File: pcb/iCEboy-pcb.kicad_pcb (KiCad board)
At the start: 2 copper layers, 51 x 61 mm, 65 parts, among them J1 DMG-CardEdge, J2 PROG_PORT, Q1 2N7002K, U1 TC74LCXR163245FT, U2 TC74LCXR163245FT, U3 ICE40UP5K-SG48ITR, U4 TPS79901DDCR, U5 TPS79901DDCR, U6 W25Q80DVSSIG, X1 SG-210STF 20MHz

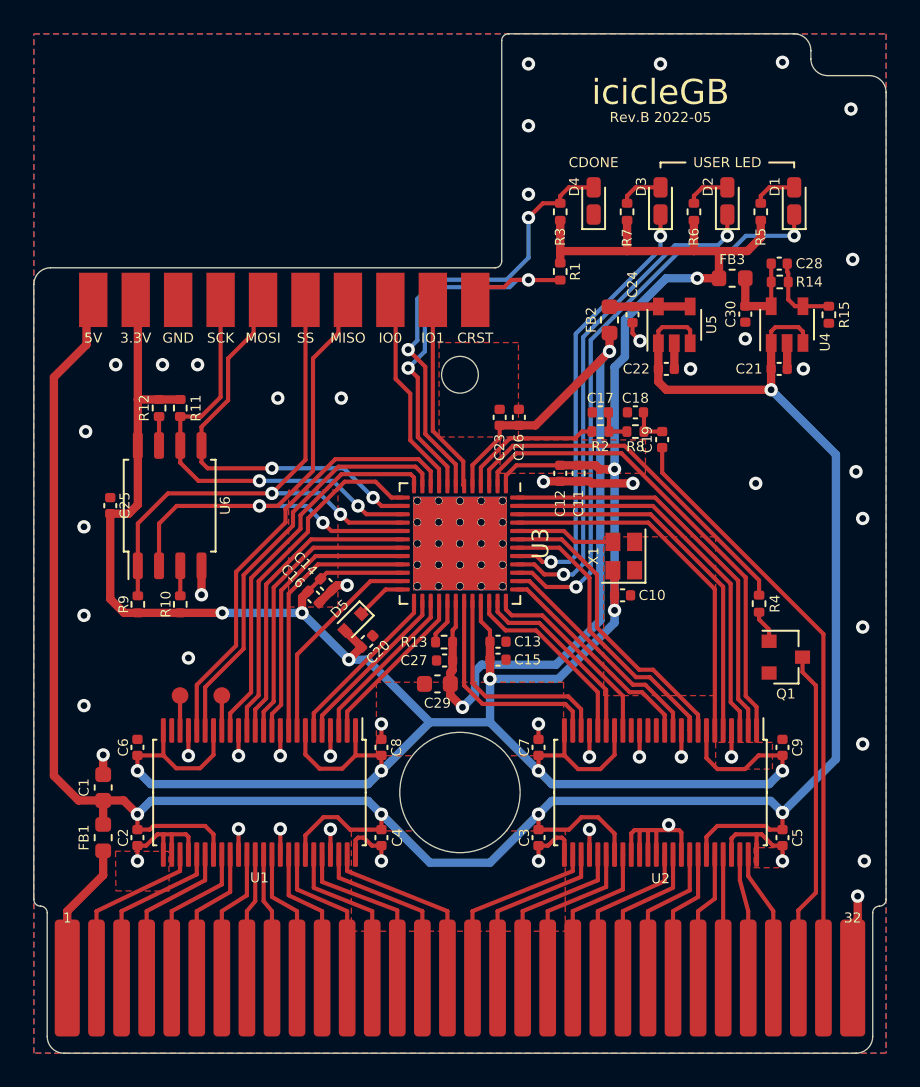
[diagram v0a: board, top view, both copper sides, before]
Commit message: update pcb, drc ok
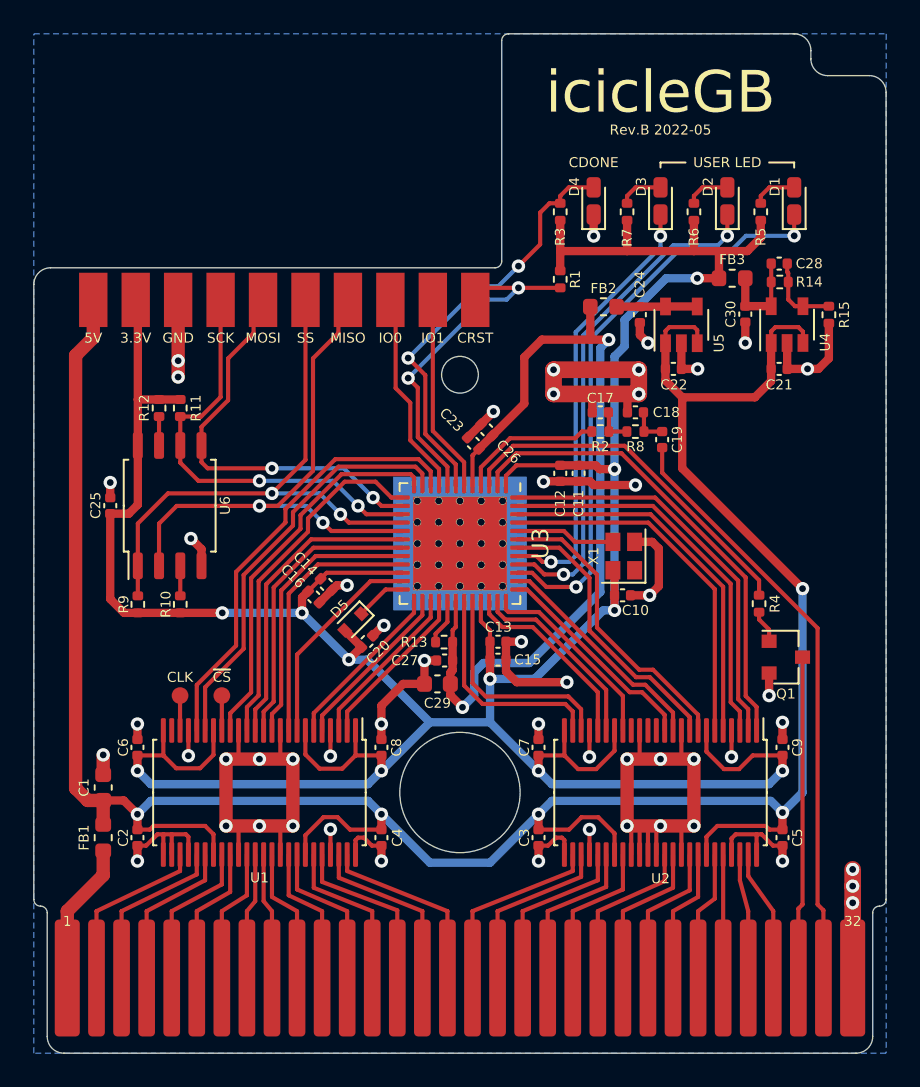
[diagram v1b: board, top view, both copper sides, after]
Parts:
- moved C23 2.21 mm to (60.8, 59.0), turned to 135 degrees
- moved C26 2.07 mm to (61.6, 58.2), turned to 135 degrees
- moved FB2 0.87 mm to (68.6, 50.8), turned to 180 degrees
- moved R1 0.46 mm to (66.0, 49.2)
- moved C24 0.44 mm to (70.8, 51.3)
- moved C22 0.42 mm to (72.8, 54.5)
- moved U5 0.42 mm to (73.2, 51.9)
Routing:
- net GND: track 72.6 -> 158.6 mm, vias 52 -> 53
- net +1V2: track 48.2 -> 50.5 mm
- net /CDONE: track 27.6 -> 25.5 mm
- net /~{CRESET}: track 23.7 -> 21.7 mm
- net +5V: track 154.7 -> 153.6 mm
- net /CB-~{RST}: track 20.0 -> 19.3 mm
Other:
- board text added: "TODO add board information silk"
- board text removed: "TODO relocation / rewiring for 1005 components add board information silk"

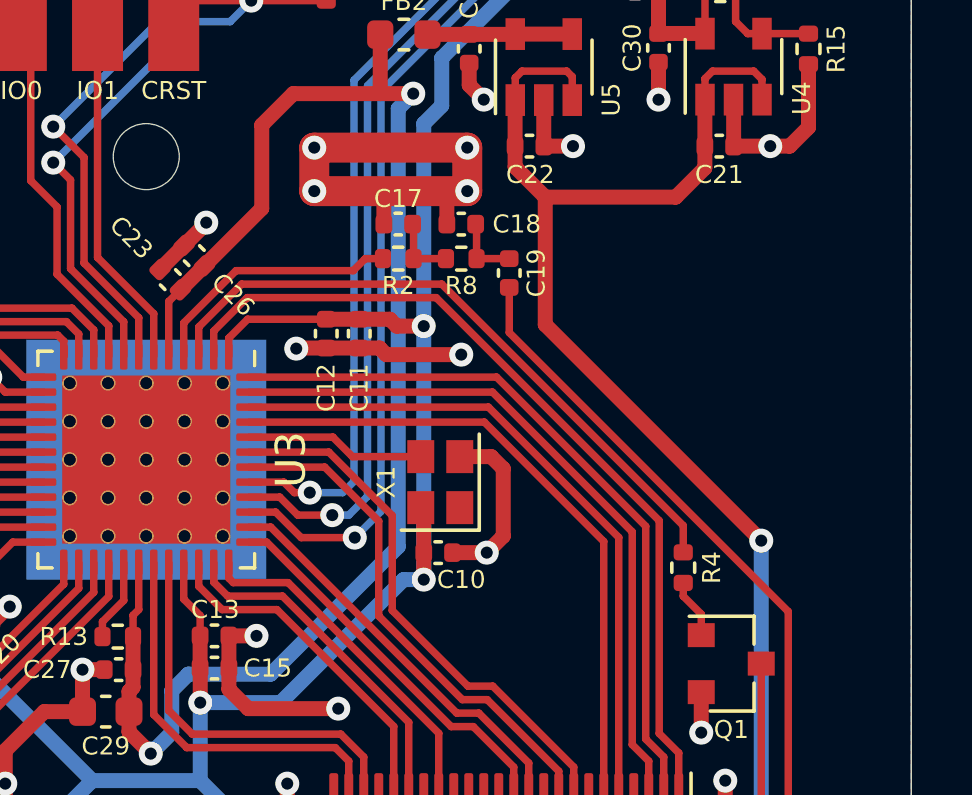
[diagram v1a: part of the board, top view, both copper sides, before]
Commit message: update board setup
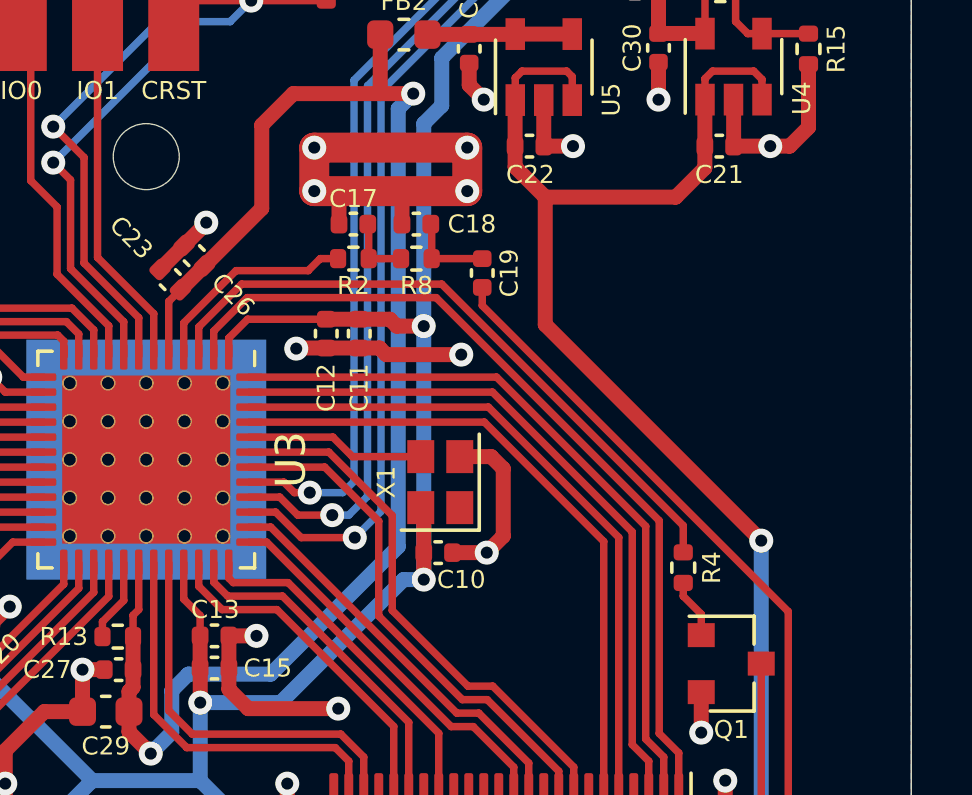
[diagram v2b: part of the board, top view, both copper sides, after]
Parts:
- moved C17 1.50 mm to (66.9, 57.1)
- moved C18 1.50 mm to (69.0, 57.1)
- moved R2 1.50 mm to (66.9, 58.3)
- moved R8 1.50 mm to (69.0, 58.3)
- moved C19 0.90 mm to (71.2, 58.8)
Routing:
- net /DV-VIN: track 8.65 -> 7.15 mm
- net Net-(C18-Pad1): track 2.25 -> 2.85 mm
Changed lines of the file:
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@@
 (kicad_pcb (version 20211014) (generator pcbnew)
   (general
-    (thickness 1.6)
+    (thickness 0.8)
   )
   (paper "A4")
+  (title_block
+    (rev "B")
+  )
   (layers
     (0 "F.Cu" signal)
-    (31 "B.Cu" signal)
+    (31 "B.Cu" power)
     (32 "B.Adhes" user "B.Adhesive")
     (33 "F.Adhes" user "F.Adhesive")
@@
       (layer "F.Mask" (type "Top Solder Mask") (thickness 0.01))
       (layer "F.Cu" (type "copper") (thickness 0.035))
-      (layer "dielectric 1" (type "core") (thickness 1.51) (material "FR4") (epsilon_r 4.5) (loss_tangent 0.02))
+      (layer "dielectric 1" (type "core") (thickness 0.71) (material "FR4") (epsilon_r 4.5) (loss_tangent 0.02))
       (layer "B.Cu" (type "copper") (thickness 0.035))
       (layer "B.Mask" (type "Bottom Solder Mask") (thickness 0.01))
       (layer "B.Paste" (type "Bottom Solder Paste"))
       (layer "B.SilkS" (type "Bottom Silk Screen"))
-      (copper_finish "None")
       (dielectric_constraints no)
+      (edge_connector yes)
     )
     (pad_to_mask_clearance 0)
@@
   )
   (footprint "Capacitor_SMD:C_0402_1005Metric" (layer "F.Cu")
-    (at 72.1 58.78 90)
+    (at 71.2 58.78 90)
     (descr "Capacitor SMD 0402 (1005 Metric), square (rectangular) end terminal, IPC_7351 nominal, (Body size source: IPC-SM-782 page 76, https://www.pcb-3d.com/wordpress/wp-content/uploads/ipc-sm-782a_amendment_1_and_2.pdf), generated with kicad-footprint-generator")
     (tags "capacitor")
@@
   )
   (footprint "Resistor_SMD:R_0402_1005Metric" (layer "F.Cu")
-    (at 68.4 58.3 180)
+    (at 66.905 58.3 180)
     (descr "Resistor SMD 0402 (1005 Metric), square (rectangular) end terminal, IPC_7351 nominal, (Body size source: IPC-SM-782 page 72, https://www.pcb-3d.com/wordpress/wp-content/uploads/ipc-sm-782a_amendment_1_and_2.pdf), generated with kicad-footprint-generator")
     (tags "resistor")
@@
   )
   (footprint "Resistor_SMD:R_0402_1005Metric" (layer "F.Cu")
-    (at 70.5 58.3 180)
+    (at 69.005 58.3 180)
     (descr "Resistor SMD 0402 (1005 Metric), square (rectangular) end terminal, IPC_7351 nominal, (Body size source: IPC-SM-782 page 72, https://www.pcb-3d.com/wordpress/wp-content/uploads/ipc-sm-782a_amendment_1_and_2.pdf), generated with kicad-footprint-generator")
     (tags "resistor")
@@
   )
   (footprint "Capacitor_SMD:C_0402_1005Metric" (layer "F.Cu")
-    (at 68.4 57.15 180)
+    (at 66.905 57.15 180)
     (descr "Capacitor SMD 0402 (1005 Metric), square (rectangular) end terminal, IPC_7351 nominal, (Body size source: IPC-SM-782 page 76, https://www.pcb-3d.com/wordpress/wp-content/uploads/ipc-sm-782a_amendment_1_and_2.pdf), generated with kicad-footprint-generator")
     (tags "capacitor")
@@
   )
   (footprint "Capacitor_SMD:C_0402_1005Metric" (layer "F.Cu")
-    (at 70.5 57.15 180)
+    (at 69.005 57.15 180)
     (descr "Capacitor SMD 0402 (1005 Metric), square (rectangular) end terminal, IPC_7351 nominal, (Body size source: IPC-SM-782 page 76, https://www.pcb-3d.com/wordpress/wp-content/uploads/ipc-sm-782a_amendment_1_and_2.pdf), generated with kicad-footprint-generator")
     (tags "capacitor")
@@
   (segment (start 70.75 83.6125) (end 70.75 81.9) (width 0.25) (layer "F.Cu") (net 2))
   (segment (start 70.21 68.1) (end 71.35 68.1) (width 0.5) (layer "F.Cu") (net 2))
-  (segment (start 70.02 57.15) (end 70.02 56.27) (width 0.5) (layer "F.Cu") (net 2))
+  (segment (start 68.525 57.15) (end 68.525 56.27) (width 0.5) (layer "F.Cu") (net 2))
   (segment (start 41.22 83.08) (end 40.7 83.08) (width 0.25) (layer "F.Cu") (net 2))
   (segment (start 79.58 54.55) (end 80.8 54.55) (width 0.5) (layer "F.Cu") (net 2))
   (segment (start 82.075 53.925) (end 81.45 54.55) (width 0.5) (layer "F.Cu") (net 2))
   (segment (start 70.7 56.05) (end 65.6 56.05) (width 1) (layer "F.Cu") (net 2))
-  (segment (start 67.92 57.15) (end 67.92 56.23) (width 0.5) (layer "F.Cu") (net 2))
+  (segment (start 66.425 57.15) (end 66.425 56.23) (width 0.5) (layer "F.Cu") (net 2))
   (segment (start 60.460589 58.660589) (end 61.260589 57.860589) (width 0.5) (layer "F.Cu") (net 2))
   (segment (start 53.75 83.6125) (end 53.75 82.75) (width 0.25) (layer "F.Cu") (net 2))
@@
   (segment (start 38.65 84.85) (end 36.5 87) (width 0.8) (layer "F.Cu") (net 6))
   (segment (start 36.5 87) (end 36.5 91) (width 0.8) (layer "F.Cu") (net 6))
-  (segment (start 61.25 60.442846) (end 62.991886 58.70096) (width 0.25) (layer "F.Cu") (net 7))
-  (segment (start 67.3 58.3) (end 67.89 58.3) (width 0.25) (layer "F.Cu") (net 7))
+  (segment (start 65.39904 58.70096) (end 65.8 58.3) (width 0.25) (layer "F.Cu") (net 7))
+  (segment (start 61.25 60.442846) (end 62.991887 58.70096) (width 0.25) (layer "F.Cu") (net 7))
+  (segment (start 62.991887 58.70096) (end 65.39904 58.70096) (width 0.25) (layer "F.Cu") (net 7))
+  (segment (start 65.8 58.3) (end 66.395 58.3) (width 0.25) (layer "F.Cu") (net 7))
   (segment (start 61.25 61.5625) (end 61.25 60.442846) (width 0.25) (layer "F.Cu") (net 7))
-  (segment (start 62.991886 58.70096) (end 66.89904 58.70096) (width 0.25) (layer "F.Cu") (net 7))
-  (segment (start 66.89904 58.70096) (end 67.3 58.3) (width 0.25) (layer "F.Cu") (net 7))
   (segment (start 38.25 87) (end 43.25 84.6) (width 0.25) (layer "F.Cu") (net 8))
   (segment (start 43.25 84.6) (end 43.25 83.6125) (width 0.25) (layer "F.Cu") (net 8))
@@
   (segment (start 80.5 86.6) (end 80.5 71.8) (width 0.25) (layer "F.Cu") (net 37))
   (segment (start 80.25 91) (end 80.25 86.85) (width 0.25) (layer "F.Cu") (net 37))
-  (segment (start 72.1 60.764282) (end 81.4 70.064282) (width 0.25) (layer "F.Cu") (net 38))
   (segment (start 81.4 70.064282) (end 81.4 86.6) (width 0.25) (layer "F.Cu") (net 38))
-  (segment (start 72.1 59.26) (end 72.1 60.764282) (width 0.25) (layer "F.Cu") (net 38))
-  (segment (start 81.75 86.95) (end 81.75 91) (width 0.25) (layer "F.Cu") (net 38))
   (segment (start 81.4 86.6) (end 81.75 86.95) (width 0.25) (layer "F.Cu") (net 38))
+  (segment (start 71.2 59.864282) (end 81.4 70.064282) (width 0.25) (layer "F.Cu") (net 38))
+  (segment (start 71.2 59.26) (end 71.2 59.864282) (width 0.25) (layer "F.Cu") (net 38))
+  (segment (start 81.75 86.95) (end 81.75 91) (width 0.25) (layer "F.Cu") (net 38))
   (segment (start 43.263 60.163) (end 43.263 59.134) (width 0.25) (layer "F.Cu") (net 39))
   (segment (start 43.263 59.134) (end 43.263 57.402) (width 0.25) (layer "F.Cu") (net 39))
@@
   (segment (start 70.163803 73.89952) (end 70.89952 73.89952) (width 0.25) (layer "F.Cu") (net 78))
   (segment (start 64.014282 67.75) (end 70.163803 73.89952) (width 0.25) (layer "F.Cu") (net 78))
-  (segment (start 68.91 58.3) (end 69.99 58.3) (width 0.25) (layer "F.Cu") (net 80))
-  (segment (start 68.91 58.3) (end 68.91 57.18) (width 0.25) (layer "F.Cu") (net 80))
-  (segment (start 68.91 57.18) (end 68.88 57.15) (width 0.25) (layer "F.Cu") (net 80))
+  (segment (start 67.415 58.3) (end 68.495 58.3) (width 0.25) (layer "F.Cu") (net 80))
+  (segment (start 67.415 58.3) (end 67.415 57.18) (width 0.25) (layer "F.Cu") (net 80))
+  (segment (start 67.415 57.18) (end 67.385 57.15) (width 0.25) (layer "F.Cu") (net 80))
   (segment (start 60.25 61.5625) (end 60.25 60.135693) (width 0.25) (layer "F.Cu") (net 83))
   (segment (start 58.376 58.261693) (end 58.376 50.421) (width 0.25) (layer "F.Cu") (net 83))
@@
   (segment (start 66.221436 64.25) (end 66.871436 64.9) (width 0.25) (layer "F.Cu") (net 90))
   (segment (start 41.993 59.134) (end 41.993 57.402) (width 0.25) (layer "F.Cu") (net 91))
-  (segment (start 71.01 57.18) (end 70.98 57.15) (width 0.25) (layer "F.Cu") (net 92))
-  (segment (start 71.01 58.3) (end 72.1 58.3) (width 0.25) (layer "F.Cu") (net 92))
-  (segment (start 71.01 58.3) (end 71.01 57.18) (width 0.25) (layer "F.Cu") (net 92))
+  (segment (start 69.515 57.18) (end 69.485 57.15) (width 0.25) (layer "F.Cu") (net 92))
+  (segment (start 69.515 58.3) (end 71.2 58.3) (width 0.25) (layer "F.Cu") (net 92))
+  (segment (start 69.515 58.3) (end 69.515 57.18) (width 0.25) (layer "F.Cu") (net 92))
   (segment (start 79.645 50.395) (end 79.645 49.35) (width 0.25) (layer "F.Cu") (net 93))
   (segment (start 79.585 48.25) (end 79.585 48.76) (width 0.25) (layer "F.Cu") (net 93))

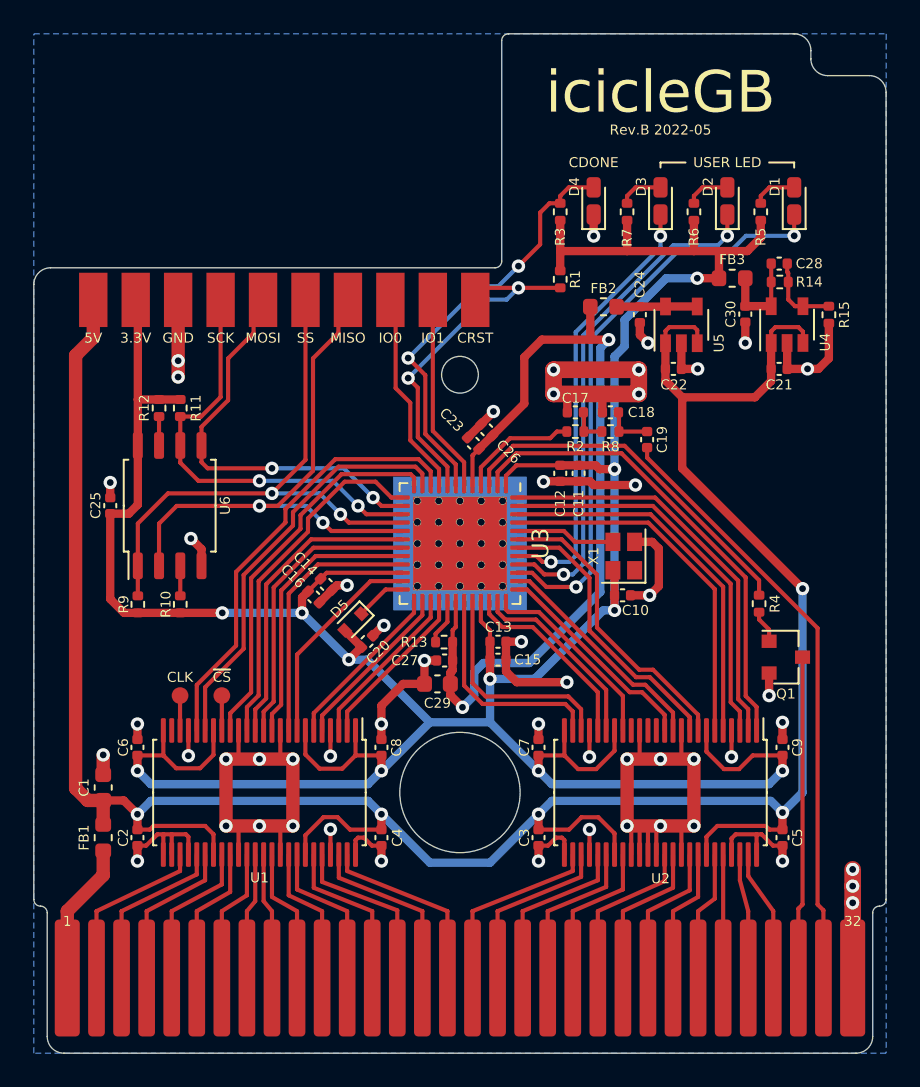
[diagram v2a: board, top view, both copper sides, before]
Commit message: change pin headers to THT, tweaking placement
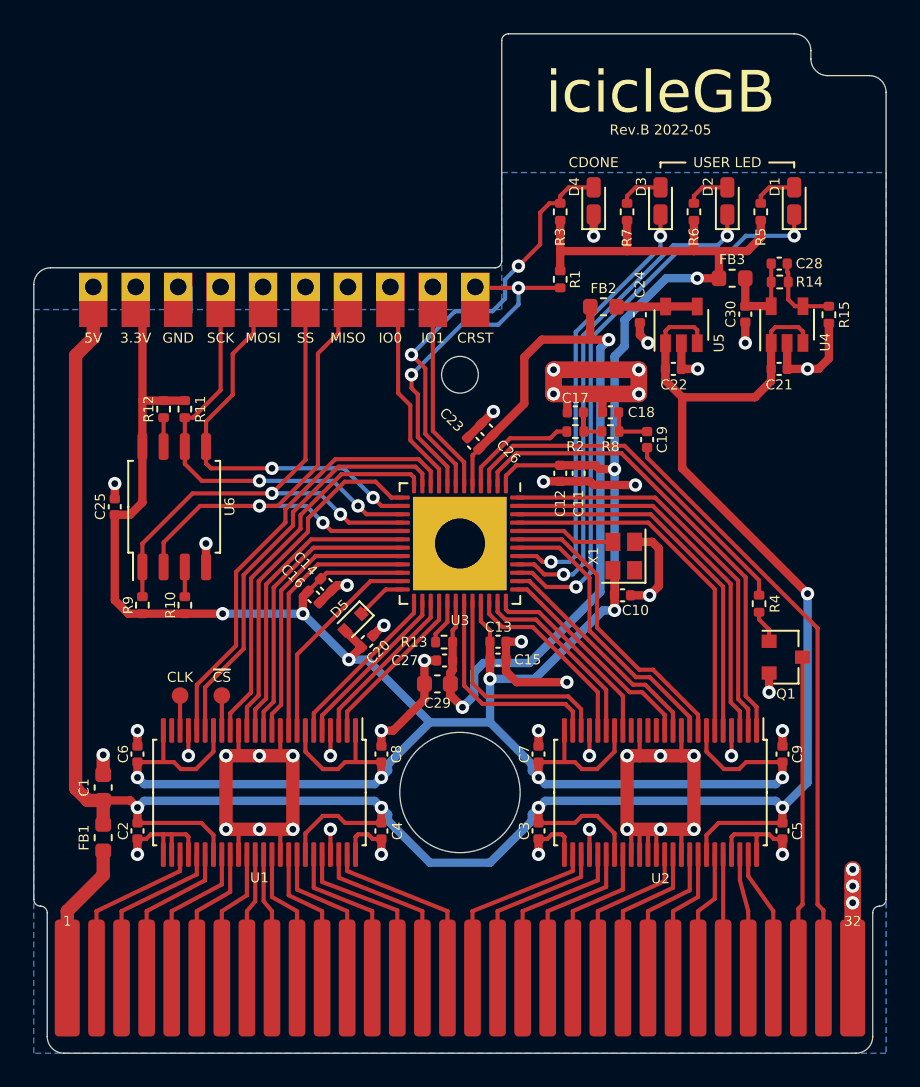
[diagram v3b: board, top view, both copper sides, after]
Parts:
- U3: footprint Package_DFN_QFN:QFN-48-1EP_7x7mm_P0.5mm_EP5.6x5.6mm_ThermalVias -> Package_DFN_QFN:QFN-48-1EP_7x7mm_P0.5mm_EP5.6x5.6mm
- moved C2 0.40 mm to (40.7, 82.2)
- moved C3 0.40 mm to (64.7, 82.2)
- moved C4 0.40 mm to (55.3, 82.2)
- moved C5 0.40 mm to (79.3, 82.2)
- moved C6 0.40 mm to (40.7, 77.6)
- moved C7 0.40 mm to (64.7, 77.6)
- moved C8 0.40 mm to (55.3, 77.6)
- moved C9 0.40 mm to (79.3, 77.6)
- moved C25 0.28 mm to (39.3, 62.8)
- moved R11 0.28 mm to (43.5, 57.0)
- moved R12 0.28 mm to (42.3, 57.0)
- moved U6 0.28 mm to (42.9, 62.8)
- moved R10 0.28 mm to (43.5, 68.7)
- moved R9 0.28 mm to (41.0, 68.7)
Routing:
- net GND: track 158.6 -> 156.2 mm, vias 53 -> 51
- net /SPI-SS: track 34.0 -> 33.1 mm
- net /SPI-MISO: track 32.5 -> 31.7 mm
- net /SPI-SCK: track 26.1 -> 25.3 mm
- net /CDONE: track 25.5 -> 26.1 mm
